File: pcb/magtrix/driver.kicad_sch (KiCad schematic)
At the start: 4 parts, among them Q2 BUK6D120

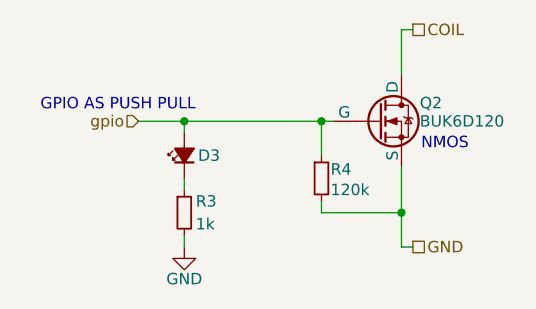
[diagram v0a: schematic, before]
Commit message: Finished schematics and footprints, need to redo the placement
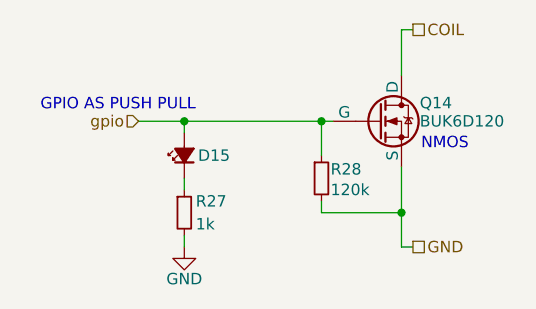
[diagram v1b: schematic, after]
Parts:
- Q14: renamed from Q2; footprint TRANSISTOR:TRANS_BUK9D23-40EX_3Dadded -> TRANSISTOR_NMOS:TRANS_BUK9D23-40EX
- renumbered D3 to D15, R3 to R27, R4 to R28
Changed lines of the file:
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@@
 		(on_board yes)
 		(dnp no)
-		(property "Reference" "R4"
+		(property "Reference" "R28"
 			(at 65.786 51.054 0)
 			(effects
@@
 		(on_board yes)
 		(dnp no)
-		(property "Reference" "D3"
+		(property "Reference" "D15"
 			(at 51.054 49.53 90)
 			(effects
@@
 		(on_board yes)
 		(dnp no)
-		(property "Reference" "Q2"
+		(property "Reference" "Q14"
 			(at 75.692 43.688 0)
 			(effects
@@
 			)
 		)
-		(property "Footprint" "TRANSISTOR:TRANS_BUK9D23-40EX_3Dadded"
+		(property "Footprint" "TRANSISTOR_NMOS:TRANS_BUK9D23-40EX"
 			(at 76.962 27.94 0)
 			(effects
@@
 		(on_board yes)
 		(dnp no)
-		(property "Reference" "R3"
+		(property "Reference" "R27"
 			(at 50.8 54.61 0)
 			(effects
@@
 		(on_board yes)
 		(dnp no)
-		(property "Reference" "#PWR08"
+		(property "Reference" "#PWR032"
 			(at 49.53 66.04 0)
 			(effects

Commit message: Added finished PCB
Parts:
- renumbered D15 to D12, Q14 to Q11, R27 to R21, R28 to R22
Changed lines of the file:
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@@
 		(on_board yes)
 		(dnp no)
-		(property "Reference" "R28"
+		(property "Reference" "R22"
 			(at 65.786 51.054 0)
 			(effects
@@
 		(instances
 			(project "magtrix"
-				(path "/11af7b42-8094-4ca6-9444-8e07a1921bec/183ed7b0-f152-4856-b3b8-9ad983ccfc71"
-					(reference "R28")
-					(unit 1)
-				)
 				(path "/11af7b42-8094-4ca6-9444-8e07a1921bec/1e80b275-0e2a-4bb9-a90b-77e94734d218"
 					(reference "R22")
@@
 					(unit 1)
 				)
-				(path "/11af7b42-8094-4ca6-9444-8e07a1921bec/8a4198c8-3d71-4373-962f-63424f827279"
-					(reference "R32")
-					(unit 1)
-				)
 				(path "/11af7b42-8094-4ca6-9444-8e07a1921bec/a751c71a-68bd-443d-b777-ca31adb4b693"
 					(reference "R6")
@@
 				(path "/11af7b42-8094-4ca6-9444-8e07a1921bec/b0f0ca87-ef09-48ab-be36-3dd097545f3c"
 					(reference "R18")
-					(unit 1)
-				)
-				(path "/11af7b42-8094-4ca6-9444-8e07a1921bec/c7b6e6ff-a63f-4e25-ada9-683d569e7e99"
-					(reference "R30")
 					(unit 1)
 				)
@@
 		(on_board yes)
 		(dnp no)
-		(property "Reference" "D15"
+		(property "Reference" "D12"
 			(at 51.054 49.53 90)
 			(effects
@@
 		(instances
 			(project "magtrix"
-				(path "/11af7b42-8094-4ca6-9444-8e07a1921bec/183ed7b0-f152-4856-b3b8-9ad983ccfc71"
-					(reference "D15")
-					(unit 1)
-				)
 				(path "/11af7b42-8094-4ca6-9444-8e07a1921bec/1e80b275-0e2a-4bb9-a90b-77e94734d218"
 					(reference "D12")
@@
 					(unit 1)
 				)
-				(path "/11af7b42-8094-4ca6-9444-8e07a1921bec/8a4198c8-3d71-4373-962f-63424f827279"
-					(reference "D17")
-					(unit 1)
-				)
 				(path "/11af7b42-8094-4ca6-9444-8e07a1921bec/a751c71a-68bd-443d-b777-ca31adb4b693"
 					(reference "D4")
@@
 				(path "/11af7b42-8094-4ca6-9444-8e07a1921bec/b0f0ca87-ef09-48ab-be36-3dd097545f3c"
 					(reference "D10")
-					(unit 1)
-				)
-				(path "/11af7b42-8094-4ca6-9444-8e07a1921bec/c7b6e6ff-a63f-4e25-ada9-683d569e7e99"
-					(reference "D16")
 					(unit 1)
 				)
@@
 		(on_board yes)
 		(dnp no)
-		(property "Reference" "Q14"
+		(property "Reference" "Q11"
 			(at 75.692 43.688 0)
 			(effects
@@
 		(instances
 			(project "magtrix"
-				(path "/11af7b42-8094-4ca6-9444-8e07a1921bec/183ed7b0-f152-4856-b3b8-9ad983ccfc71"
-					(reference "Q14")
-					(unit 1)
-				)
 				(path "/11af7b42-8094-4ca6-9444-8e07a1921bec/1e80b275-0e2a-4bb9-a90b-77e94734d218"
 					(reference "Q11")
@@
 					(unit 1)
 				)
-				(path "/11af7b42-8094-4ca6-9444-8e07a1921bec/8a4198c8-3d71-4373-962f-63424f827279"
-					(reference "Q16")
-					(unit 1)
-				)
 				(path "/11af7b42-8094-4ca6-9444-8e07a1921bec/a751c71a-68bd-443d-b777-ca31adb4b693"
 					(reference "Q3")
@@
 				(path "/11af7b42-8094-4ca6-9444-8e07a1921bec/b0f0ca87-ef09-48ab-be36-3dd097545f3c"
 					(reference "Q9")
-					(unit 1)
-				)
-				(path "/11af7b42-8094-4ca6-9444-8e07a1921bec/c7b6e6ff-a63f-4e25-ada9-683d569e7e99"
-					(reference "Q15")
 					(unit 1)
 				)
@@
 		(on_board yes)
 		(dnp no)
-		(property "Reference" "R27"
+		(property "Reference" "R21"
 			(at 50.8 54.61 0)
 			(effects
@@
 		(instances
 			(project "magtrix"
-				(path "/11af7b42-8094-4ca6-9444-8e07a1921bec/183ed7b0-f152-4856-b3b8-9ad983ccfc71"
-					(reference "R27")
-					(unit 1)
-				)
 				(path "/11af7b42-8094-4ca6-9444-8e07a1921bec/1e80b275-0e2a-4bb9-a90b-77e94734d218"
 					(reference "R21")
@@
 					(unit 1)
 				)
-				(path "/11af7b42-8094-4ca6-9444-8e07a1921bec/8a4198c8-3d71-4373-962f-63424f827279"
-					(reference "R31")
-					(unit 1)
-				)
 				(path "/11af7b42-8094-4ca6-9444-8e07a1921bec/a751c71a-68bd-443d-b777-ca31adb4b693"
 					(reference "R5")
@@
 				(path "/11af7b42-8094-4ca6-9444-8e07a1921bec/b0f0ca87-ef09-48ab-be36-3dd097545f3c"
 					(reference "R17")
-					(unit 1)
-				)
-				(path "/11af7b42-8094-4ca6-9444-8e07a1921bec/c7b6e6ff-a63f-4e25-ada9-683d569e7e99"
-					(reference "R29")
 					(unit 1)
 				)
@@
 		(on_board yes)
 		(dnp no)
-		(property "Reference" "#PWR032"
+		(property "Reference" "#PWR029"
 			(at 49.53 66.04 0)
 			(effects
@@
 		(instances
 			(project "magtrix"
-				(path "/11af7b42-8094-4ca6-9444-8e07a1921bec/183ed7b0-f152-4856-b3b8-9ad983ccfc71"
-					(reference "#PWR032")
-					(unit 1)
-				)
 				(path "/11af7b42-8094-4ca6-9444-8e07a1921bec/1e80b275-0e2a-4bb9-a90b-77e94734d218"
 					(reference "#PWR029")
@@
 					(unit 1)
 				)
-				(path "/11af7b42-8094-4ca6-9444-8e07a1921bec/8a4198c8-3d71-4373-962f-63424f827279"
-					(reference "#PWR034")
-					(unit 1)
-				)
 				(path "/11af7b42-8094-4ca6-9444-8e07a1921bec/a751c71a-68bd-443d-b777-ca31adb4b693"
 					(reference "#PWR07")
@@
 					(unit 1)
 				)
-				(path "/11af7b42-8094-4ca6-9444-8e07a1921bec/c7b6e6ff-a63f-4e25-ada9-683d569e7e99"
-					(reference "#PWR033")
-					(unit 1)
-				)
